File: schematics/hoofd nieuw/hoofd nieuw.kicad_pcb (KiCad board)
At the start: 2 copper layers, 170 x 75 mm, 36 parts, among them J1 Conn_01x04_Pin, J2 Conn_01x02_Pin, J3 SFR02, J4 Conn_01x04_Pin, U1 ATtiny402-SS

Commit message: plaats de componenten grofweg
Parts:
- J4: value Conn_01x04_Pin -> Conn_01x03_Pin; footprint Connector_PinHeader_2.54mm:PinHeader_1x04_P2.54mm_Vertical -> Connector_PinHeader_2.54mm:PinHeader_1x03_P2.54mm_Vertical
- moved D15 77.9 mm to (171.7, 46.6)
- moved D16 77.9 mm to (171.7, 53.3)
- moved D17 77.9 mm to (179.8, 33.4)
- moved D18 77.9 mm to (179.8, 40.0)
- moved D19 77.9 mm to (179.8, 46.6)
- moved D20 77.9 mm to (179.8, 53.3)
- moved D13 74.0 mm to (152.3, 75.8)
- moved J1 70.0 mm to (147.1, 34.4)
- moved D12 69.4 mm to (146.9, 83.1)
- moved C2 66.4 mm to (135.6, 38.0), turned to 180 degrees
- moved D11 66.1 mm to (137.8, 84.3)
- moved D14 66.0 mm to (152.9, 66.5)
- moved D10 63.9 mm to (128.7, 84.4)
- moved D9 61.0 mm to (118.2, 82.0)
- moved C1 60.3 mm to (129.7, 37.2)
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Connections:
- C1 pad 1: Net-(J4-Pin_3) -> +3.3V
- J4 pad 3: Net-(J4-Pin_3) -> +3.3V
- U1 pad 1: Net-(J4-Pin_3) -> +3.3V

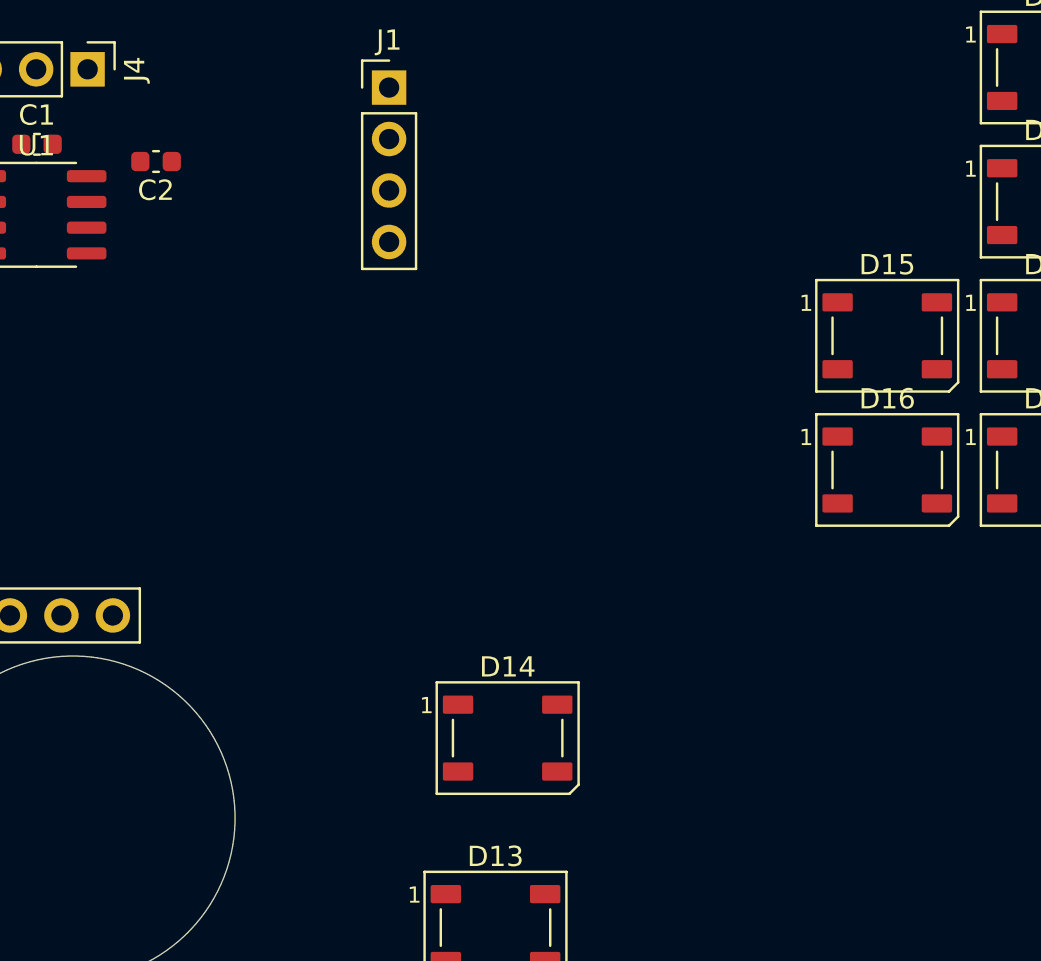
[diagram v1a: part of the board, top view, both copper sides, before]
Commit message: voeg de ontbrekende foodprints toe
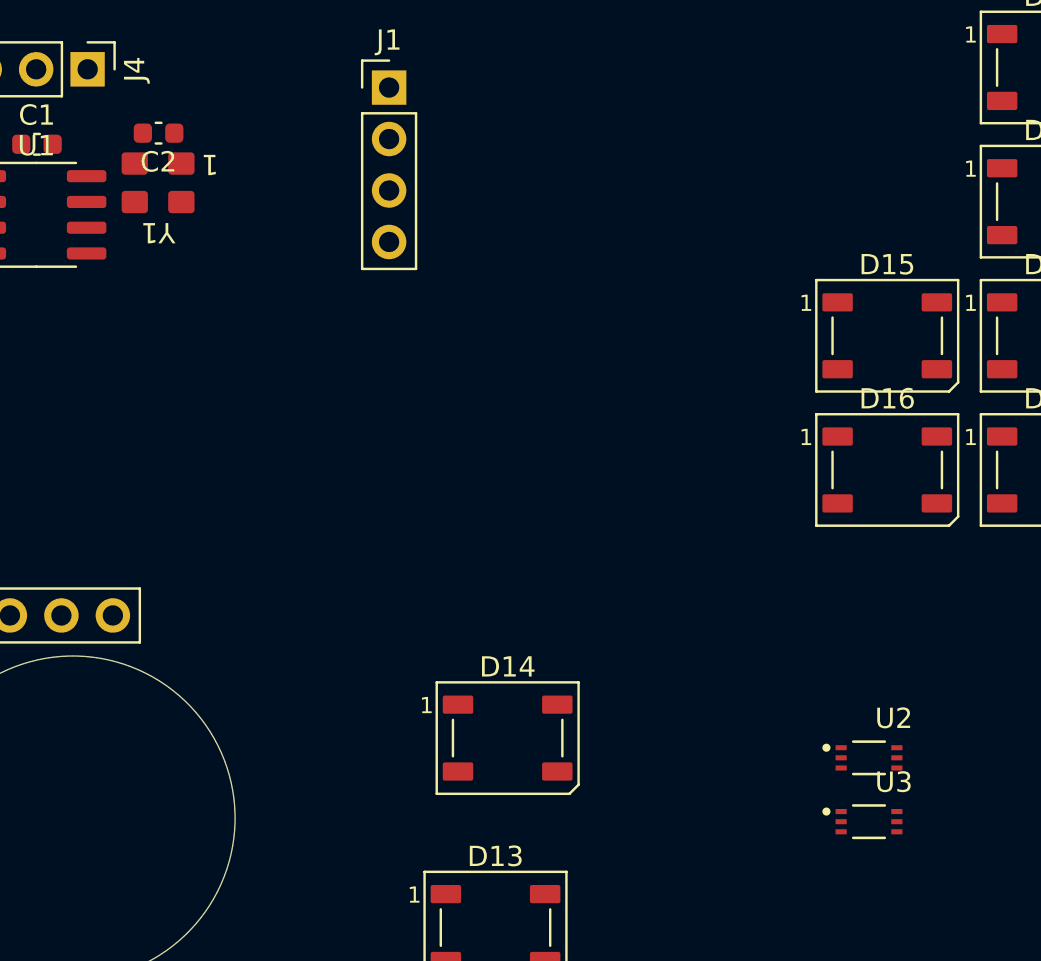
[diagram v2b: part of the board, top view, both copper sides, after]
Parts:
- added U2: BH1750FVI-TR, BH1750FVI-TR:XDCR_BH1750FVI-TR, F.Cu at (170.8, 67.5)
- added U3: BH1750FVI-TR, BH1750FVI-TR:XDCR_BH1750FVI-TR, F.Cu at (170.8, 70.6)
- added Y1: ECS-2333MV-100-BN-TR, Oscillator:ESC-2333-xxx-xxx, F.Cu at (135.7, 39.1)
- moved C2 1.41 mm to (135.7, 36.6)

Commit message: teken alles waarvan ik de locate ken of niet belangrijk is (absolut)
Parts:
- moved C3 115.1 mm to (187.1, 55.4)
- moved U3 87.8 mm to (83.1, 75.0)
- moved U2 87.7 mm to (83.1, 70.5)
- moved C4 50.4 mm to (121.3, 73.0)
- moved C8 14.3 mm to (79.7, 74.7), turned to -90 degrees
- moved C7 13.8 mm to (80.0, 70.3), turned to -90 degrees
- moved C5 7.82 mm to (71.6, 57.1)
- moved R2 6.24 mm to (121.3, 47.0), turned to 90 degrees
- moved J1 5.74 mm to (143.8, 39.1)
- moved C6 4.92 mm to (94.9, 70.5), turned to 90 degrees
- moved R1 4.32 mm to (94.9, 73.5), turned to 90 degrees
- moved J4 0.90 mm to (132.2, 34.4)
- moved D21 0.59 mm to (121.3, 42.0)
- moved C2 0.28 mm to (135.4, 36.6)
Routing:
- net /SDA: track 0.00 -> 35.6 mm, vias 0 -> 2
- net +3.3V: track 0.00 -> 31.9 mm, vias 0 -> 2
- net /SCL: track 0.00 -> 31.4 mm
- net /UPDI/~{RESET}: track 0.00 -> 8.55 mm
- net Net-(D21-K): track 0.00 -> 6.06 mm
- net /XTAL: track 0.00 -> 2.38 mm
- net Net-(D1-DIN): track 0.00 -> 2.18 mm
- net GND: vias 0 -> 3
- added copper zone on F.Cu, net +3.3V
- added copper zone on B.Cu, net GND
- added copper zone on F.Cu, net GND

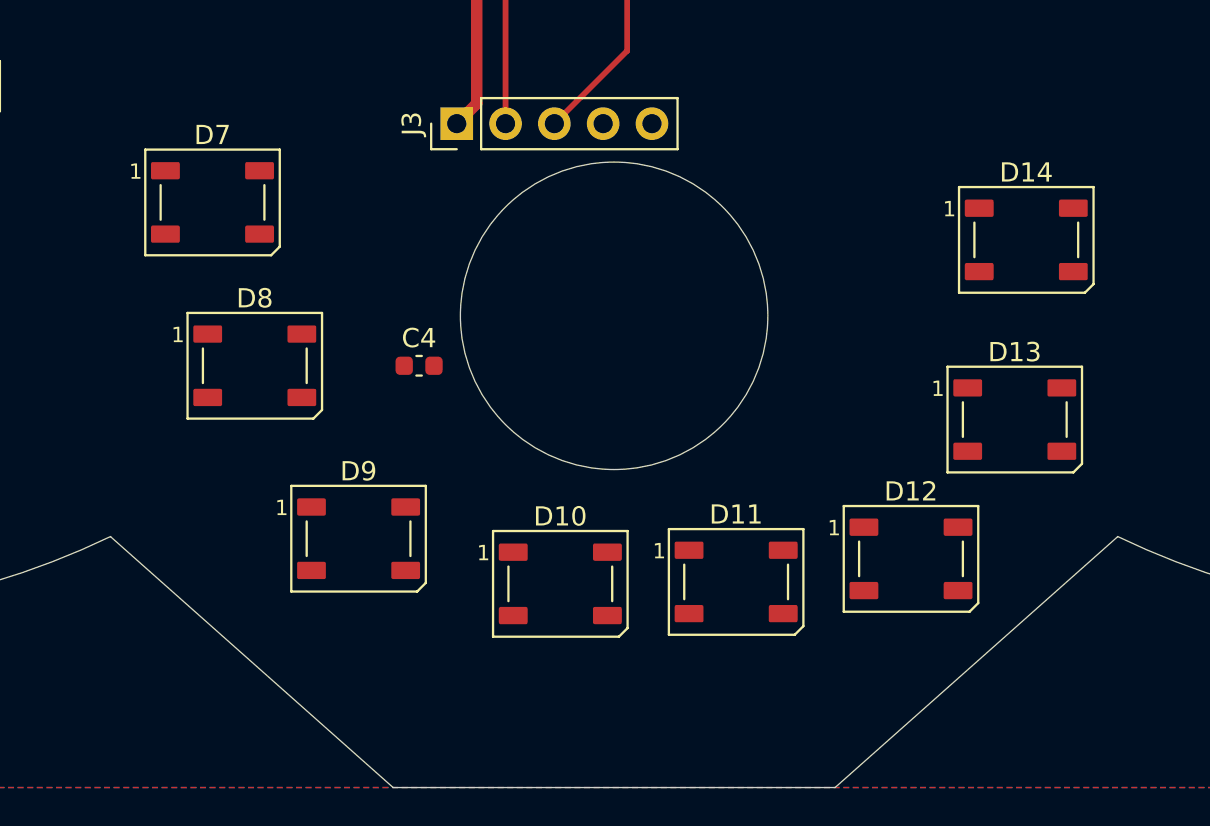
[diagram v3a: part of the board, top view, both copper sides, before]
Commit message: led van het 'mondje' zijn geplaatst
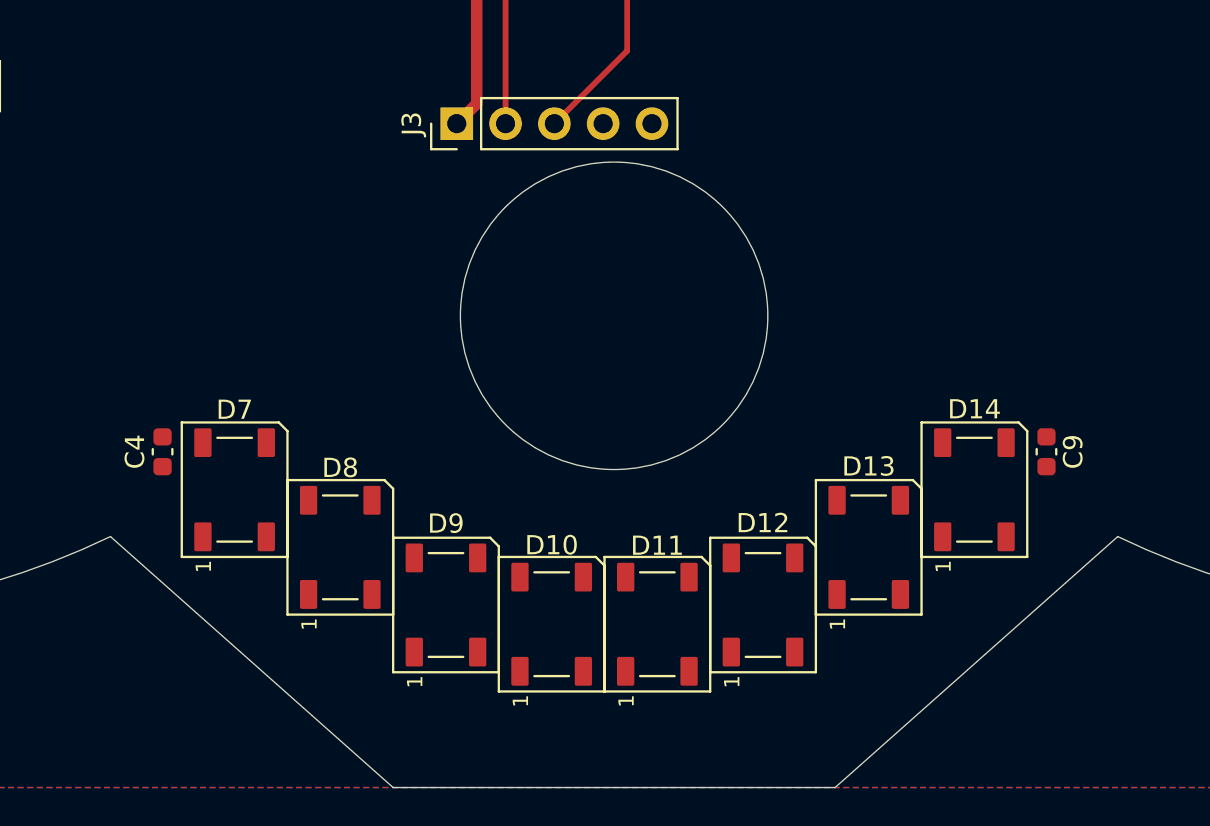
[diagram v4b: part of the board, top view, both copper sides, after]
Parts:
- added C9: 1µF, Capacitor_SMD:C_0603_1608Metric, F.Cu at (154.0, 77.5)
- moved D7 15.0 mm to (111.8, 79.5), turned to 90 degrees
- moved C4 14.1 mm to (108.0, 77.5), turned to 90 degrees
- moved D14 13.3 mm to (150.2, 79.5), turned to 90 degrees
- moved D8 10.4 mm to (117.2, 82.5), turned to 90 degrees
- moved D13 10.1 mm to (144.8, 82.5), turned to 90 degrees
- moved D12 8.07 mm to (139.2, 85.5), turned to 90 degrees
- moved D9 5.71 mm to (122.8, 85.5), turned to 90 degrees
- moved D11 4.65 mm to (133.8, 86.5), turned to 90 degrees
- moved D10 2.15 mm to (128.2, 86.5), turned to 90 degrees

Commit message: de locatie van alle componenten is bepaald in het hoofd
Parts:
- removed D20, D6: WS2812B, LED_SMD:LED_WS2812B_PLCC4_5.0x5.0mm_P3.2mm
- moved C8 89.0 mm to (168.4, 68.3)
- moved U3 88.7 mm to (171.5, 68.0)
- moved D5 44.6 mm to (104.5, 66.0)
- moved D1 40.7 mm to (106.8, 47.0)
- moved C5 38.4 mm to (109.7, 52.5)
- moved D17 32.1 mm to (185.2, 65.0)
- moved C3 29.4 mm to (162.2, 71.2)
- moved D4 29.4 mm to (85.5, 75.0)
- moved D19 24.6 mm to (155.2, 47.3)
- moved D15 23.4 mm to (158.5, 66.0)
- moved D3 22.5 mm to (76.8, 65.0)
- moved D16 22.5 mm to (177.5, 75.0)
- moved J2 18.0 mm to (115.7, 52.0), turned to 90 degrees
- moved D2 16.8 mm to (86.2, 38.5)
- moved U2 8.75 mm to (91.5, 68.0)
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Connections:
- D19 pad 2: Net-(D19-DOUT) -> unconnected-(D19-DOUT-Pad2)
- D7 pad 4: Net-(D6-DOUT) -> Net-(D5-DOUT)
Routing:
- net Net-(D13-DOUT): track 0.00 -> 8.81 mm
- net Net-(D12-DOUT): track 0.00 -> 8.81 mm
- net Net-(D11-DOUT): track 0.00 -> 6.81 mm
- net Net-(D10-DOUT): track 0.00 -> 5.81 mm
- net Net-(D10-DIN): track 0.00 -> 4.81 mm
- net Net-(D8-DOUT): track 0.00 -> 2.99 mm
- net Net-(D7-DOUT): track 0.00 -> 2.99 mm
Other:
- outline, holes or cut-outs redrawn

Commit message: nieuw hoofd is klaar
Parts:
- moved R1 61.5 mm to (147.5, 41.5), turned to -90 degrees
- moved C6 58.7 mm to (147.5, 44.5), turned to -90 degrees
- moved C4 5.39 mm to (111.8, 73.7), turned to 0 degrees
- moved C5 2.79 mm to (107.0, 51.9), turned to -90 degrees
- moved J2 0.20 mm to (115.5, 52.0)
- turned D15 to 180 degrees
- turned D16 to 180 degrees
- turned D17 to 180 degrees
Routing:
- net +5V: track 0.00 -> 325.0 mm, vias 0 -> 2
- net Net-(U2-DVI): track 0.00 -> 107.3 mm, vias 0 -> 6
- net /SDA: track 35.6 -> 127.8 mm, vias 2 -> 9
- net /SCL: track 31.4 -> 119.2 mm, vias 0 -> 5
- net +3.3V: track 31.9 -> 113.6 mm
- net Net-(D17-DOUT): track 0.00 -> 31.2 mm
- net Net-(D4-DOUT): track 0.00 -> 29.3 mm
- net Net-(D2-DOUT): track 0.00 -> 25.1 mm
- net Net-(D1-DOUT): track 0.00 -> 20.5 mm
- net Net-(D15-DOUT): track 0.00 -> 19.2 mm
- net Net-(D18-DOUT): track 0.00 -> 18.1 mm
- net Net-(D3-DOUT): track 0.00 -> 17.1 mm
- net Net-(D14-DOUT): track 0.00 -> 16.0 mm
- net Net-(D5-DOUT): track 0.00 -> 12.7 mm
- net Net-(D1-DIN): track 2.18 -> 14.6 mm
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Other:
- outline, holes or cut-outs redrawn

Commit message: maak de gbr file's voor nieuw hoofd
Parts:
- added D20: ~, Library:D5V0P4B5LP08, F.Cu at (134.4, 41.7)
- added D6: PESD5V0X1BCSFYL, PESD5V0X1BCSFYL:PMEG3005AESFYL, F.Cu at (116.1, 54.3)
- added R3: 5K1, Resistor_SMD:R_0603_1608Metric, F.Cu at (129.7, 35.7)
- moved J4 1.25 mm to (132.2, 33.1)
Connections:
- J4 pad 2: /UPDI/~{RESET} -> Net-(J4-Pin_2)
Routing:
- net Net-(J4-Pin_2): track 0.00 -> 2.82 mm
- net +3.3V: track 113.6 -> 116.3 mm
- net /SDA: track 127.8 -> 128.7 mm, vias 9 -> 10
- net /SCL: track 119.2 -> 120.0 mm
